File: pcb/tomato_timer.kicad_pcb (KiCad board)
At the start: 2 copper layers, 68.6 x 53.3 mm, 26 parts, among them J1 External_Power, Q1 BSS138, Q2 BSS138, SW1 SW_SPDT, SW2 SW_Reset, SW3 SW_Start, SW4 SW_Stop, U1 XBeeSeries1

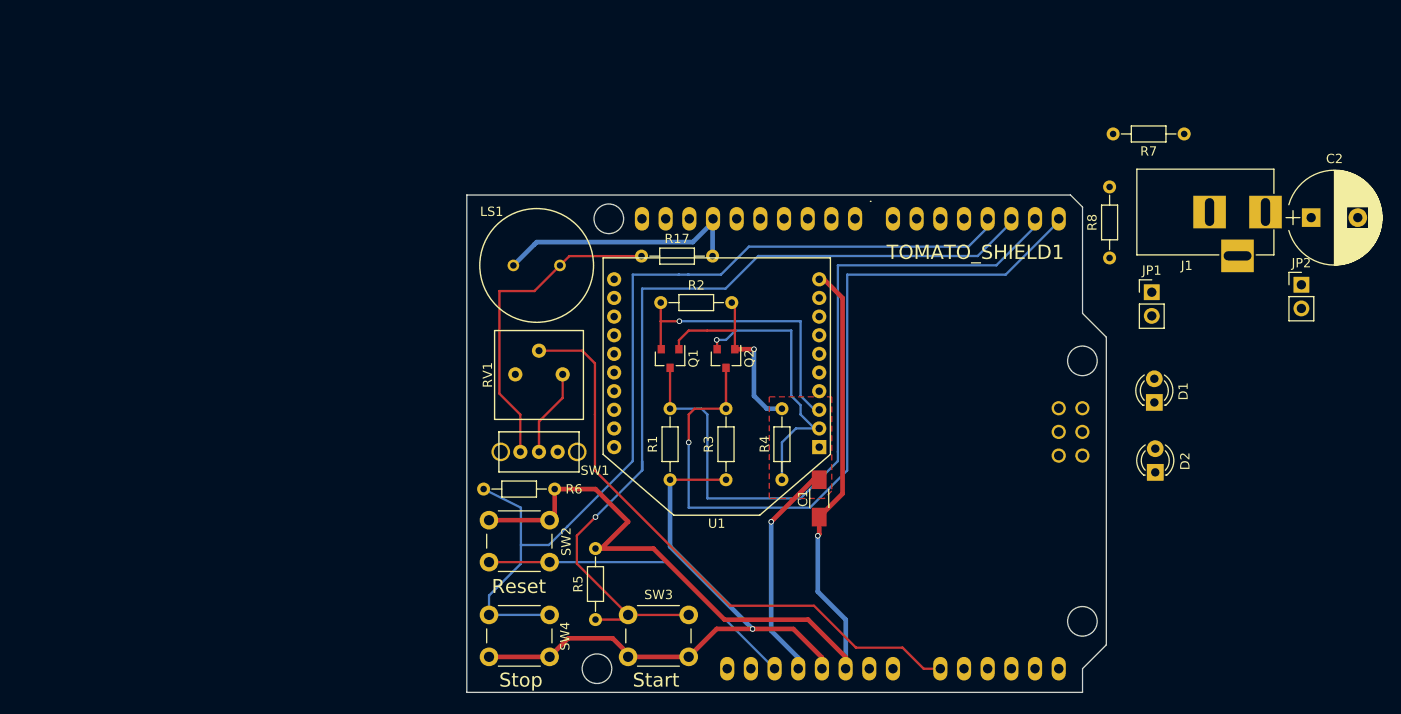
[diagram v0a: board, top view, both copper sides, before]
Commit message: Added basic footprints for neopixel ring and neopixel strip terminal block.
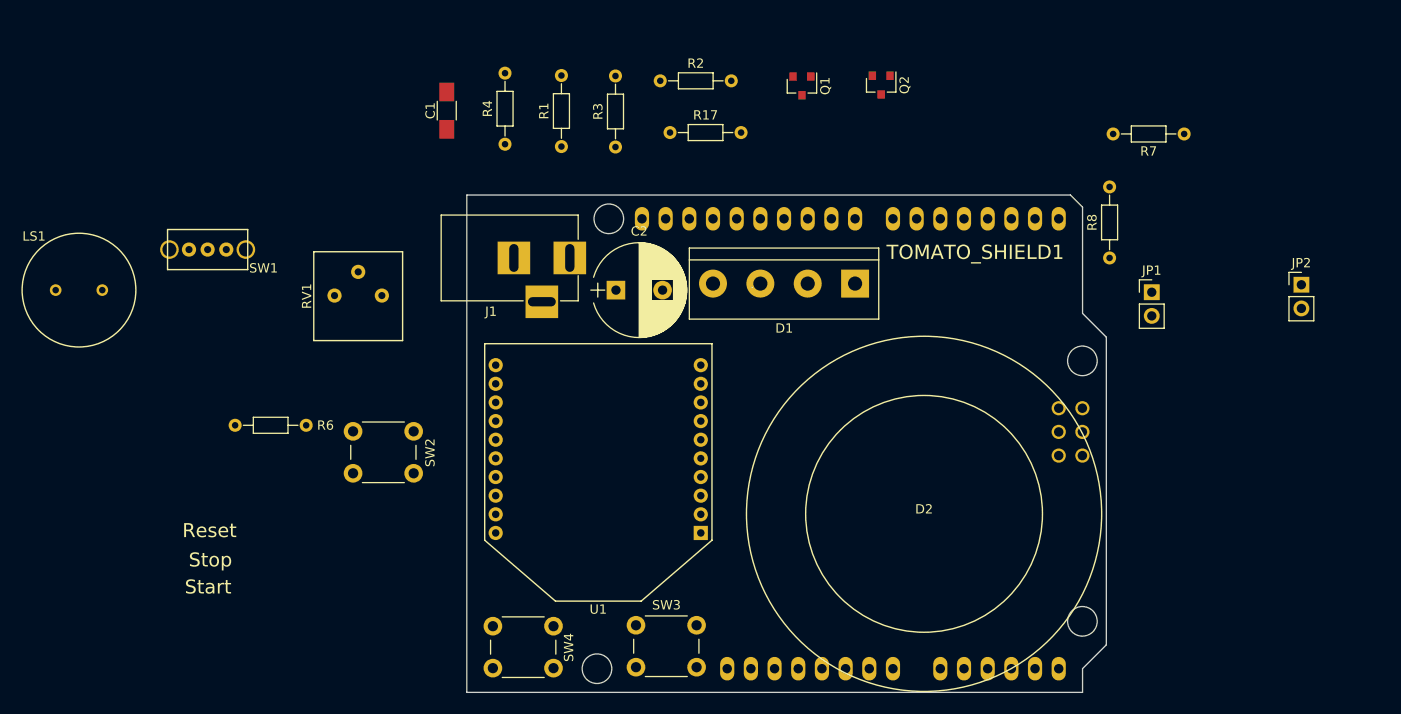
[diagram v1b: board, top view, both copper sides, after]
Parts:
- removed R5: 10K, Resistors_THT:R_Axial_DIN0204_L3.6mm_D1.6mm_P7.62mm_Horizontal
- D1: footprint LEDs:LED_D3.0mm -> Terminal_Blocks:TerminalBlock_bornier-4_P5.08mm
- D2: footprint LEDs:LED_D3.0mm -> tomato-timer:NeoPixelRing_12
- moved C2 75.0 mm to (164.6, 71.2)
- moved J1 74.8 mm to (159.6, 67.7)
- moved C1 57.7 mm to (146.4, 51.9)
- moved LS1 49.2 mm to (107.0, 71.2)
- moved R4 46.7 mm to (152.7, 55.5)
- moved SW1 41.6 mm to (120.8, 66.8)
- moved R3 37.6 mm to (164.5, 55.8)
- moved R1 37.6 mm to (158.7, 55.8)
- moved D1 34.5 mm to (190.2, 70.5), turned to 180 degrees
- moved Q2 33.7 mm to (193.0, 49.1)
- moved Q1 32.5 mm to (184.5, 49.2)
- moved R6 27.5 mm to (123.7, 85.7)
- moved D2 25.2 mm to (197.6, 95.2), turned to 180 degrees
- moved R2 23.8 mm to (169.3, 48.7)
- moved RV1 21.2 mm to (136.9, 71.8)
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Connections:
- R2 pad 1: (no net) -> /DIN
- R4 pad 1: (no net) -> /DOUT
- R8 pad 1: (no net) -> Net-(D1-Pad4)
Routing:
- net /GND1: track 103.1 -> 0.00 mm, vias 1 -> 0
- net /BTN_STOP: track 100.8 -> 0.00 mm
- net /BTN_START: track 95.3 -> 0.00 mm, vias 1 -> 0
- net /RX: track 84.0 -> 0.00 mm, vias 1 -> 0
- net /TX: track 78.4 -> 0.00 mm
- net Net-(RV1-Pad2): track 73.3 -> 0.00 mm
- net /5V: track 67.1 -> 0.00 mm, vias 1 -> 0
- net /3V3: track 48.3 -> 0.00 mm, vias 2 -> 0
- net /RESET: track 35.4 -> 0.00 mm
- net Net-(LS1-Pad2): track 35.0 -> 0.00 mm
- net /DIN: track 30.6 -> 0.00 mm, vias 1 -> 0
- net /DOUT: track 30.6 -> 0.00 mm, vias 1 -> 0
- net /GND3: track 27.4 -> 0.00 mm
- net (no net): track 0.92 -> 0.00 mm
- net /GND2: track 0.64 -> 0.00 mm
- removed copper zone on F.Cu, net /3V3

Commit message: Removed switch for external PS, and added pads to neopixel footprint.
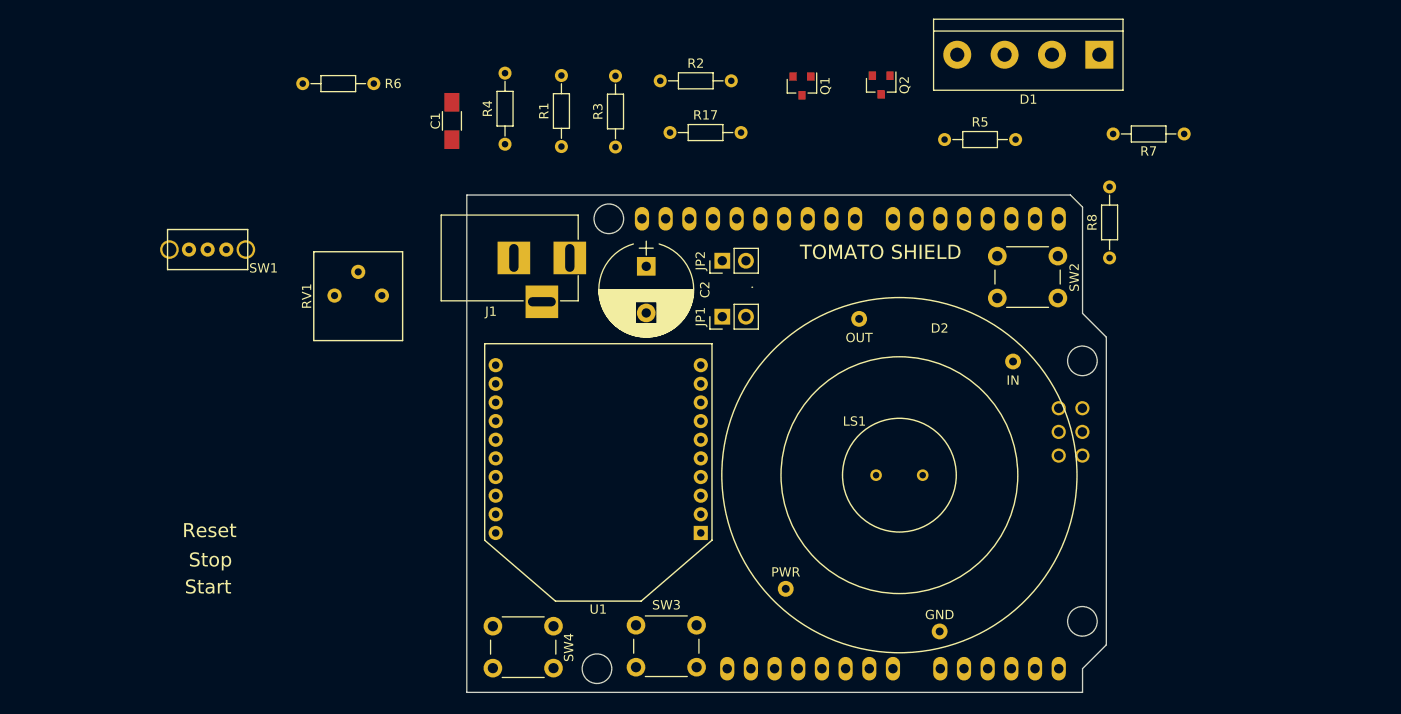
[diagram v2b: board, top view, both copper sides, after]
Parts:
- added R5: 10K, Resistors_THT:R_Axial_DIN0204_L3.6mm_D1.6mm_P7.62mm_Horizontal, F.Cu at (199.8, 55.0)
- TOMATO SHIELD: renamed from TOMATO_SHIELD1
- moved LS1 90.2 mm to (195.0, 91.0)
- moved SW2 71.6 mm to (212.0, 72.0)
- moved JP2 62.2 mm to (176.0, 68.0), turned to 90 degrees
- moved JP1 46.1 mm to (176.0, 74.0), turned to 90 degrees
- moved R6 37.4 mm to (131.0, 49.0)
- moved D1 35.9 mm to (216.4, 45.9)
- moved D2 4.92 mm to (195.0, 91.0), turned to 0 degrees
- moved C2 4.13 mm to (167.8, 68.6), turned to 270 degrees
- moved C1 1.23 mm to (147.0, 53.0)
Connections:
- C2 pad 1: Net-(C2-Pad1) -> /5V_IN
- C2 pad 2: Net-(C2-Pad2) -> /GND_IN
- D1 pad 2: Net-(C2-Pad2) -> /GND_IN
- D1 pad 3: Net-(C2-Pad1) -> /5V_IN
- J1 pad 1: Net-(C2-Pad1) -> /5V_IN
- J1 pad 2: Net-(C2-Pad2) -> /GND_IN
- JP1 pad 1: Net-(C2-Pad2) -> /GND_IN
- JP2 pad 1: Net-(C2-Pad1) -> /5V_IN
- R7 pad 1: (no net) -> Net-(D2-Pad4)

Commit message: Re-worked the volume potentiometer for the buzzer.
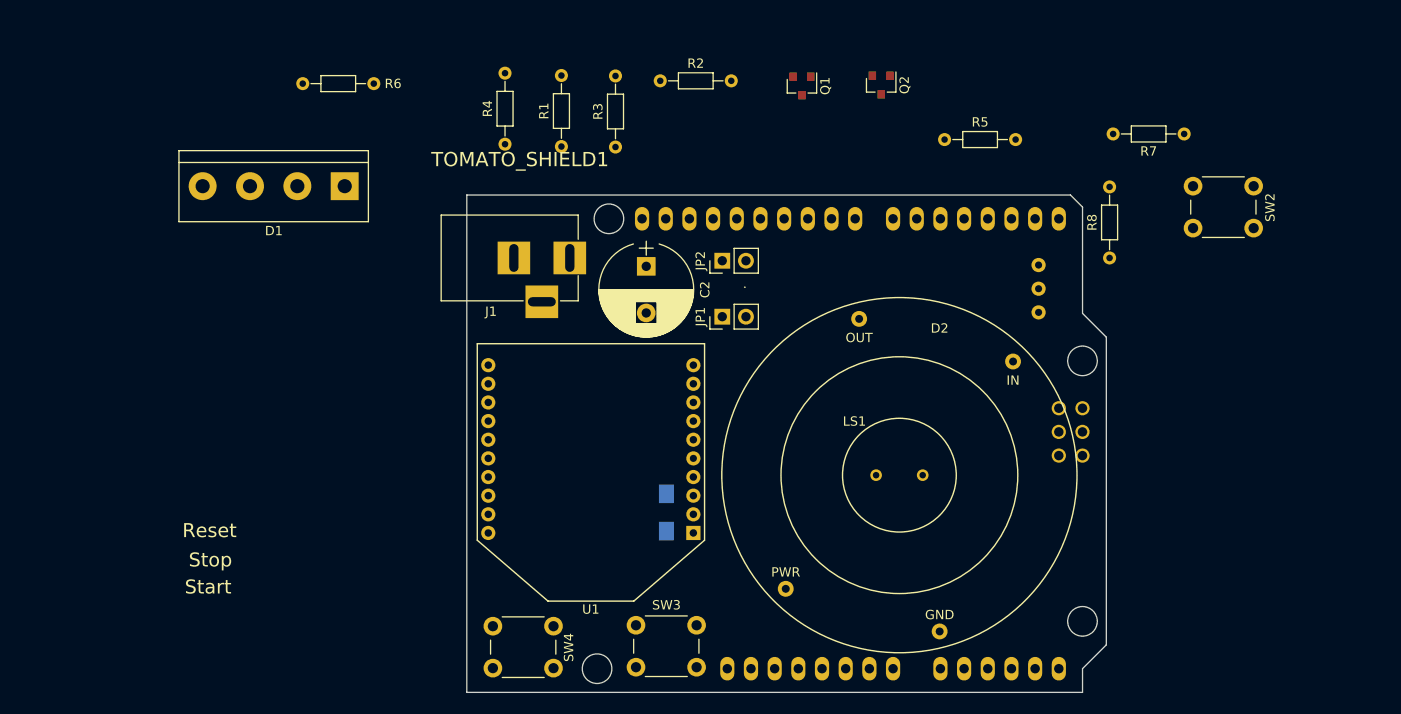
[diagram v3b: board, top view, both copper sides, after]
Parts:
- removed R17: 1K, Resistors_THT:R_Axial_DIN0204_L3.6mm_D1.6mm_P7.62mm_Horizontal
- removed SW1: SW_SPDT, tomato_timer:Tomato_SPDT_Switch
- removed TOMATO SHIELD: ARDUINO_SHIELD, freetronics_footprints:ARDUINO_SHIELD
- added TOMATO_SHIELD1: ARDUINO_SHIELD, freetronics_footprints:ARDUINO_SHIELD, F.Cu at (148.6, 114.3)
- C1: moved to B.Cu
- RV1: value POT -> 10K; footprint tomato_timer:Bourns_3310P_Potentiometer -> tomato-timer:Whell_Potentiometer_3352T; moved to B.Cu
- moved D1 82.2 mm to (135.5, 60.0)
- moved RV1 75.9 mm to (212.8, 71.0), turned to 90 degrees
- moved C1 47.9 mm to (170.0, 95.0), turned to 270 degrees
- moved SW2 22.3 mm to (233.0, 64.5)
- moved U1 0.80 mm to (161.9, 88.7)
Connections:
- RV1 pad 1: /BUZZER -> /GND3
- RV1 pad 2: Net-(RV1-Pad2) -> Net-(LS1-Pad2)
- RV1 pad 3: (no net) -> /BUZZER

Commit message: Picked remaning part footprints, and prepared board layout.
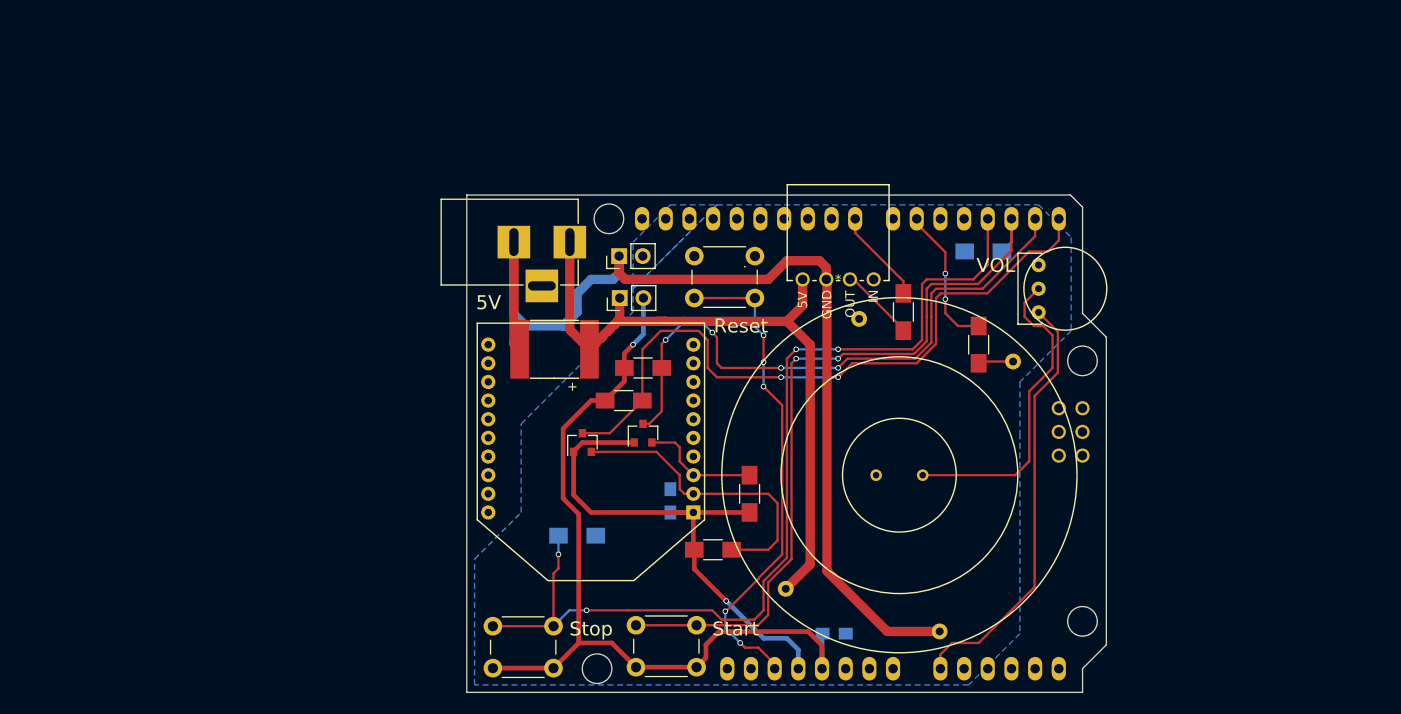
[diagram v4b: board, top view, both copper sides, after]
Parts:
- added C3: 0.1uF, Capacitors_SMD:C_0805_HandSoldering, B.Cu at (188.0, 108.0)
- C1: footprint Capacitors_SMD:C_1206_HandSoldering -> Capacitors_SMD:C_0805_HandSoldering
- C2: footprint Capacitors_THT:CP_Radial_D10.0mm_P5.00mm -> tomato-timer:SMD-2824
- D1: footprint Terminal_Blocks:TerminalBlock_bornier-4_P5.08mm -> tomato-timer:SSW-104-02-G-S-RA_4POS_Female_Header
- R1, R2, R3, R4, R7, R8: footprint Resistors_THT:R_Axial_DIN0204_L3.6mm_D1.6mm_P7.62mm_Horizontal -> Resistors_SMD:R_1206_HandSoldering
- R5, R6: footprint Resistors_THT:R_Axial_DIN0204_L3.6mm_D1.6mm_P7.62mm_Horizontal -> Resistors_SMD:R_1206_HandSoldering; moved to B.Cu
- RV1: moved to F.Cu
- moved R6 56.7 mm to (160.4, 97.5)
- moved SW2 54.0 mm to (179.5, 72.0)
- moved D1 53.9 mm to (188.4, 70.0), turned to 0 degrees
- moved Q2 50.0 mm to (161.0, 87.5), turned to 90 degrees
- moved R4 48.9 mm to (175.0, 99.0), turned to 180 degrees
- moved R2 45.3 mm to (178.9, 93.0), turned to 270 degrees
- moved Q1 41.0 mm to (167.5, 86.5), turned to 90 degrees
- moved R7 31.6 mm to (203.5, 77.0), turned to 90 degrees
- moved R3 27.2 mm to (165.4, 83.0), turned to 0 degrees
- moved R1 25.3 mm to (167.5, 79.5), turned to 0 degrees
- moved R8 22.9 mm to (195.4, 73.5)
- moved C2 13.3 mm to (158.0, 77.5), turned to 180 degrees
- moved JP1 12.8 mm to (164.9, 67.5)
- moved R5 12.7 mm to (204.0, 67.0), turned to 180 degrees
- moved JP2 11.7 mm to (165.0, 72.0)
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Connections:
- C1 pad 1: /GND1 -> /GND
- JP1 pad 2: /GND2 -> /GND
- LS1 pad 1: /GND3 -> /GND
- R5 pad 2: /GND1 -> /GND
- R6 pad 2: /GND1 -> /GND
- RV1 pad 1: /GND3 -> /GND
- SW2 pad 2: /GND1 -> /GND
- TOMATO_SHIELD1 pad GND1: /GND1 -> /GND
- TOMATO_SHIELD1 pad GND2: /GND2 -> /GND
- TOMATO_SHIELD1 pad GND3: /GND3 -> /GND
- U1 pad 10: /GND1 -> /GND
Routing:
- net /GND_IN: track 0.00 -> 109.5 mm
- net /BTN_STOP: track 0.00 -> 102.7 mm, vias 0 -> 4
- net /5V: track 0.00 -> 88.9 mm, vias 0 -> 1
- net /BTN_START: track 0.00 -> 81.9 mm, vias 0 -> 2
- net /5V_IN: track 0.00 -> 74.4 mm
- net /RX: track 0.00 -> 74.0 mm, vias 0 -> 2
- net /TX: track 0.00 -> 65.4 mm, vias 0 -> 4
- net /3V3: track 0.00 -> 56.6 mm, vias 0 -> 1
- net /RESET: track 0.00 -> 53.1 mm, vias 0 -> 5
- net /BUZZER: track 0.00 -> 46.0 mm
- net Net-(LS1-Pad2): track 0.00 -> 34.0 mm
- net /DOUT: track 0.00 -> 32.5 mm
- net /PIXEL_RING_PIN: track 0.00 -> 15.5 mm, vias 0 -> 2
- net /DIN: track 0.00 -> 12.8 mm
- net /PIXEL_STRIP_PIN: track 0.00 -> 10.1 mm
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- added copper zone on B.Cu, net /GND
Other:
- net class LED_Power added: clearance 0.4, trace_width 1, via_dia 0.6, via_drill 0.4
- board text added: "5V"
- board text added: "GND"
- board text added: "IN"
- board text added: "OUT"
- board text added: "VOL"

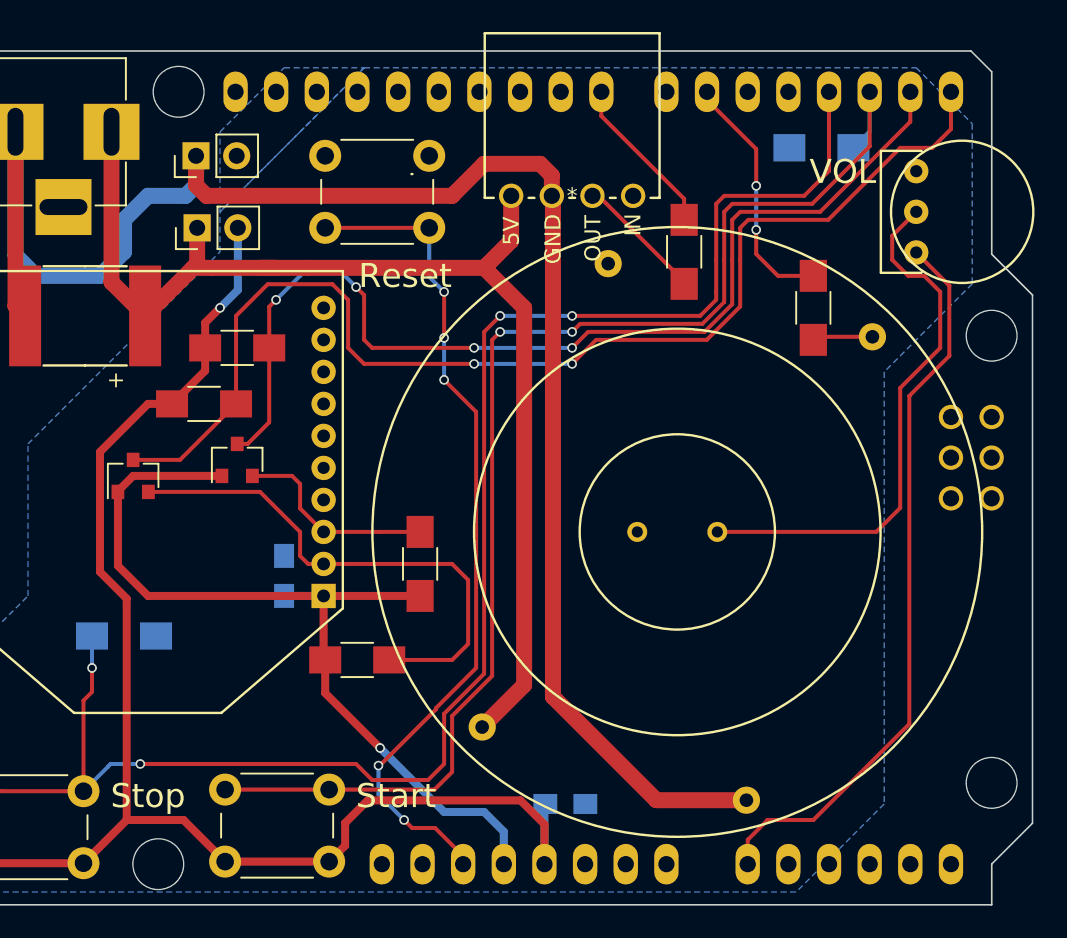
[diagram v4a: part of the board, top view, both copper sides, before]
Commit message: Converted the buzzer to be controlled by a transistor and volume control by the pot wiper.
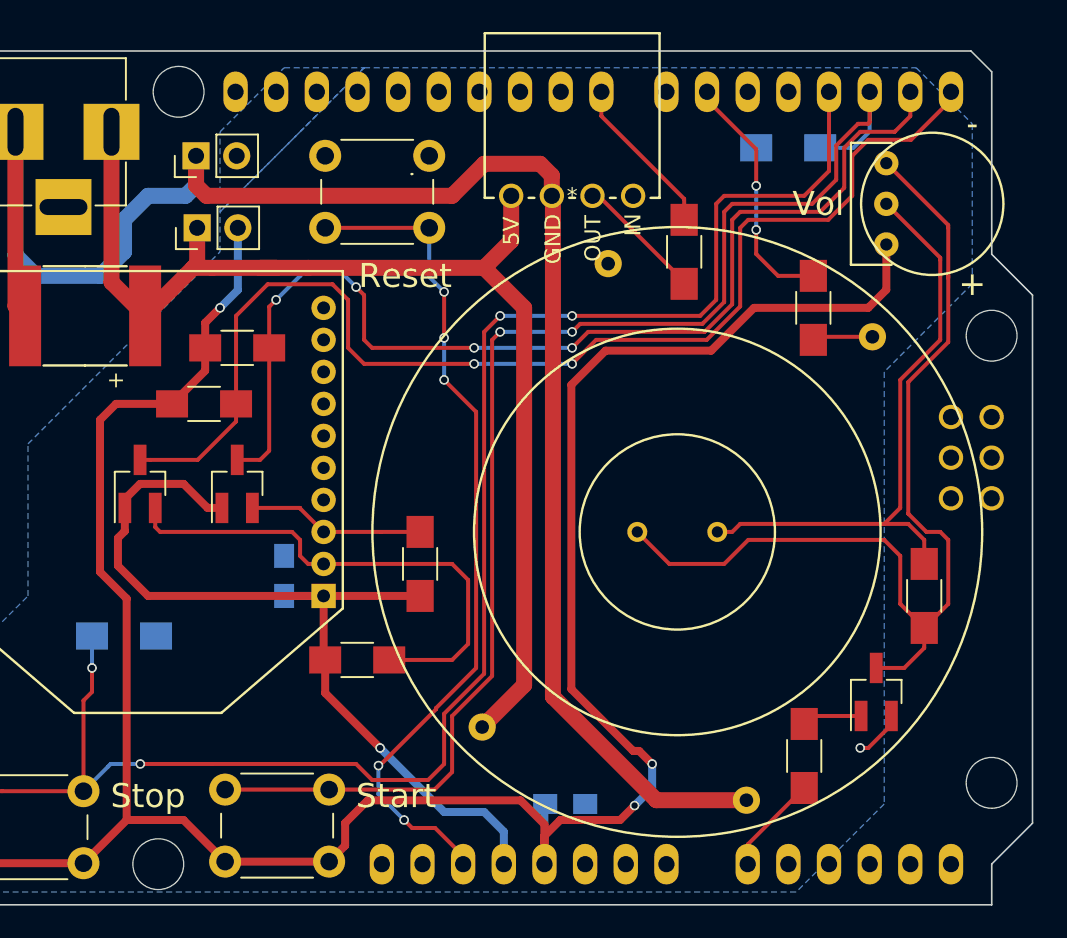
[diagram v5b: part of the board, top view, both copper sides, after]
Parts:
- added Q3: TRANSISTOR_NPN, tomato-timer:MMBT6428LT1G_NPN, F.Cu at (207.4, 101.0)
- added R10: 1K, Resistors_SMD:R_1206_HandSoldering, F.Cu at (210.4, 95.0)
- added R9: 10K, Resistors_SMD:R_1206_HandSoldering, F.Cu at (202.9, 105.0)
- Q1, Q2: footprint TO_SOT_Packages_SMD:SOT-23 -> TO_SOT_Packages_SMD:SOT-23_Handsoldering
- moved R5 2.07 mm to (201.9, 67.0)
- moved RV1 1.94 mm to (210.9, 70.5)
- moved Q1 1.50 mm to (167.5, 88.0)
- moved Q2 0.66 mm to (161.4, 88.0)
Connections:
- LS1 pad 1: /GND -> Net-(LS1-Pad1)
- RV1 pad 1: /GND -> Net-(LS1-Pad1)
- RV1 pad 3: /BUZZER -> /5V
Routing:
- net /5V: track 88.9 -> 152.3 mm, vias 1 -> 3
- net Net-(LS1-Pad1): track 0.00 -> 62.2 mm
- net /BUZZER: track 46.0 -> 6.22 mm
- net Net-(LS1-Pad2): track 34.0 -> 37.9 mm
- net Net-(Q3-PadB): track 0.00 -> 3.76 mm
- net /GND: track 0.00 -> 3.10 mm, vias 0 -> 1
- net /TX: track 65.4 -> 68.1 mm
- net /BTN_START: track 81.9 -> 84.4 mm
- net /DIN: track 12.8 -> 11.1 mm
- net /RX: track 74.0 -> 74.6 mm
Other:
- board text added: "+"
- board text added: "-"
- board text added: "Vol"
- board text removed: "VOL"
